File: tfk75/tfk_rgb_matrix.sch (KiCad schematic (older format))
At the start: 1 part

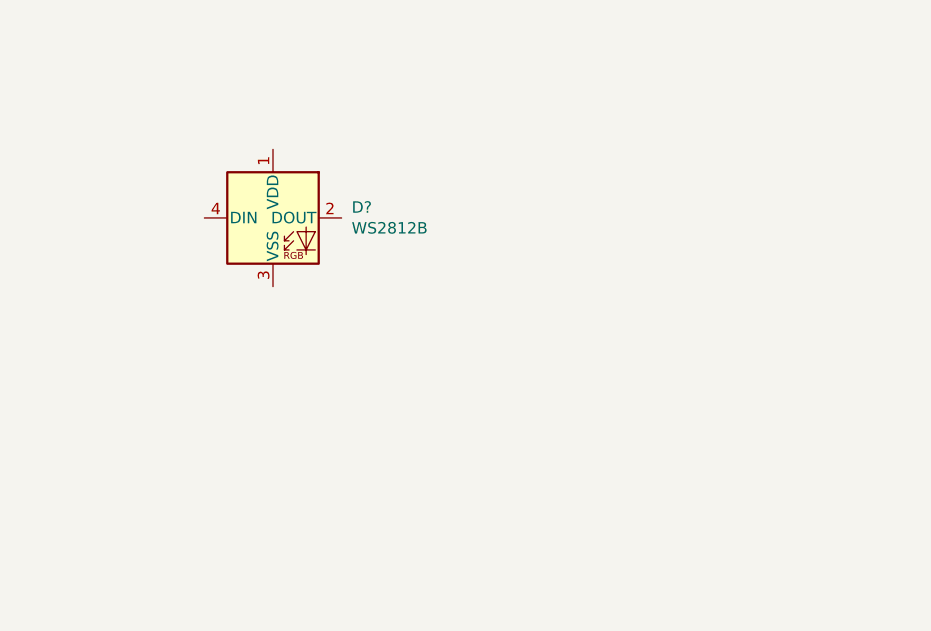
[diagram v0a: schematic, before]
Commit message: Begin RGB matrix
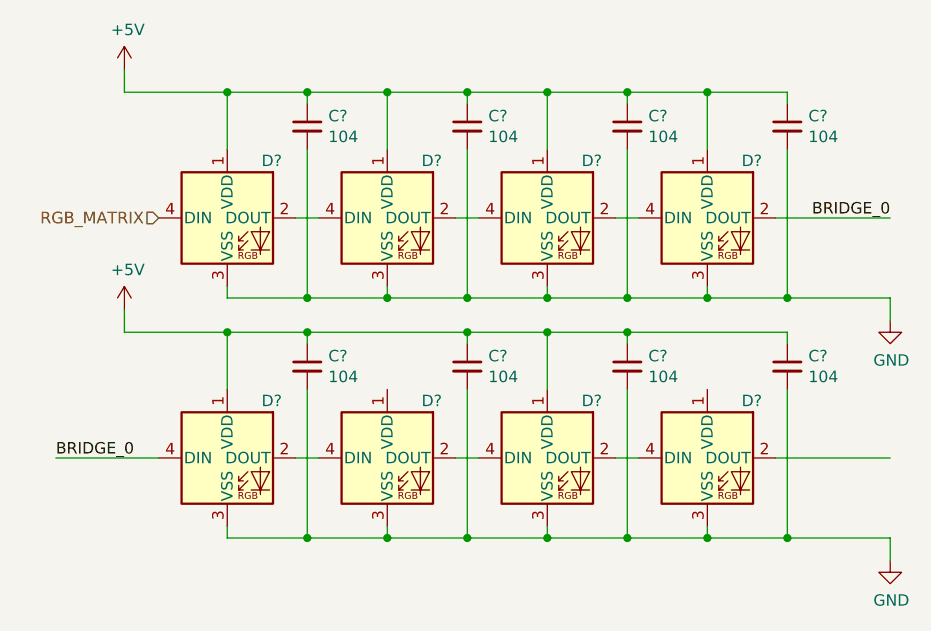
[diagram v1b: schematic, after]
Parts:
- added C? (x8): 104, symbol Device:C_Small
- added D? (x7): WS2812B, LED_SMD:LED_WS2812B_PLCC4_5.0x5.0mm_P3.2mm, symbol LED:WS2812B
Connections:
- net +5V: now reaches D?.1 (VDD)
- net +5V: now also C?.1, C?.1, C?.1, C?.1, C?.1, C?.1, C?.1, C?.1, D?.1 (VDD), D?.1 (VDD), D?.1 (VDD), D?.1 (VDD), D?.1 (VDD)
- net at D?.2 (DOUT): now also D?.4 (DIN)
- net GND: now reaches D?.3 (VSS)
- net GND: now also C?.2, C?.2, C?.2, C?.2, C?.2, C?.2, C?.2, C?.2, D?.3 (VSS), D?.3 (VSS), D?.3 (VSS), D?.3 (VSS), D?.3 (VSS), D?.3 (VSS), D?.3 (VSS)
- net RGB_MATRIX: now reaches D?.4 (DIN)
- new net: D?.2 (DOUT), D?.4 (DIN) (x5)
- new net BRIDGE_0: D?.2 (DOUT), D?.4 (DIN)
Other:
- moved on the sheet: D?
